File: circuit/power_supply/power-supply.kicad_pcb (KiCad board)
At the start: 2 copper layers, 21 parts, among them P1 CONN_2, U1 MCS34063A

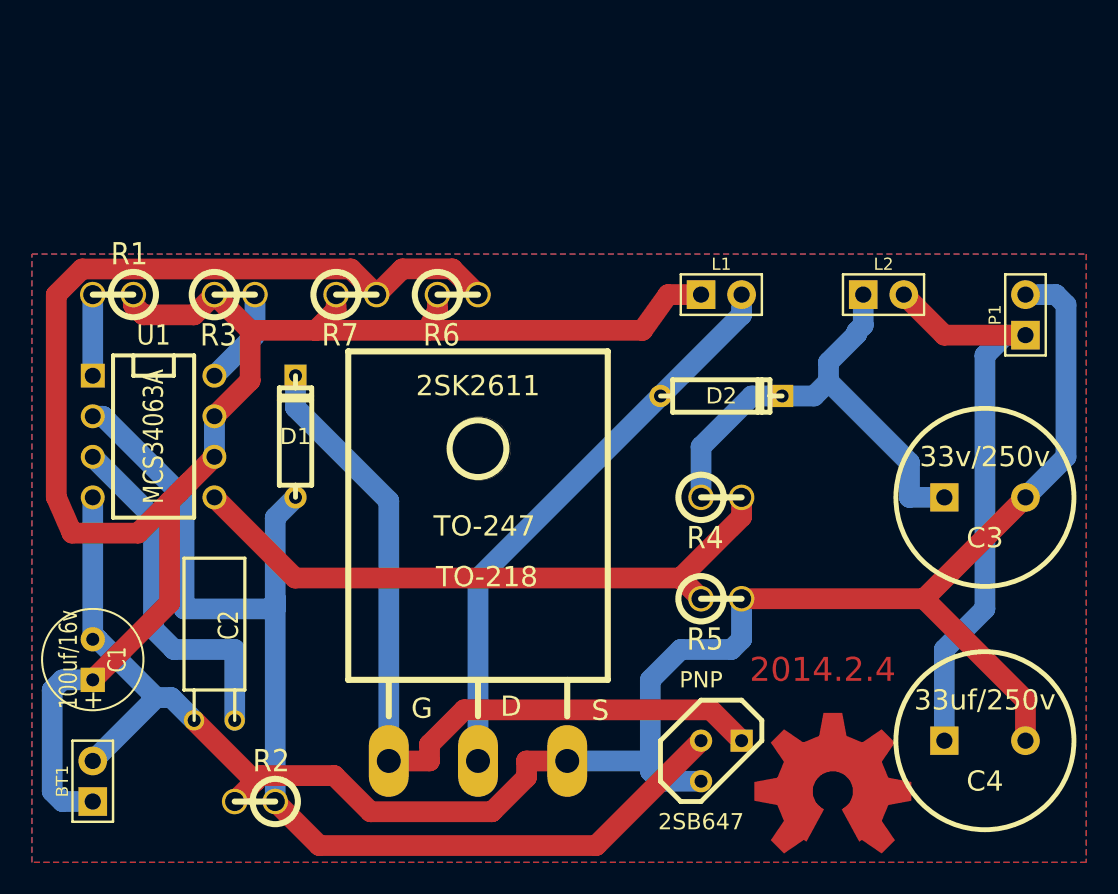
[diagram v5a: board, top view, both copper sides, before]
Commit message: power_supply: expanded the pad size
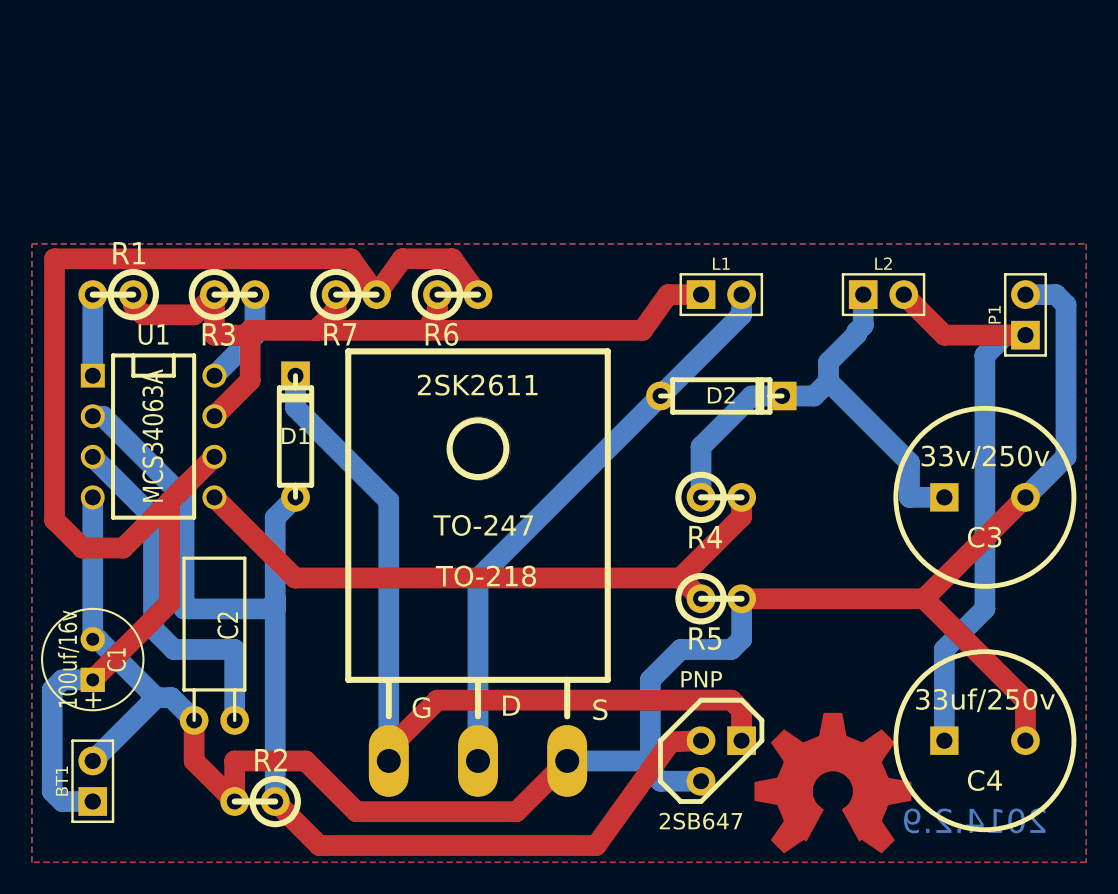
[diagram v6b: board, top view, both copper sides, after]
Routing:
- net N-0000011: track 80.2 -> 84.6 mm
- net N-000007: track 124.2 -> 126.6 mm
- net N-000004: track 51.4 -> 52.8 mm
- net N-000009: track 52.4 -> 51.8 mm
- net N-000008: track 71.9 -> 72.5 mm
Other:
- net class width 1.0 added: clearance 0.254, trace_width 1, via_dia 0.889, via_drill 0.635
- board text added: "2014.2.9"
- board text removed: "2014.2.4"

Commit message: power_supply: fixed the wrong TO-92 ECB footprint issue
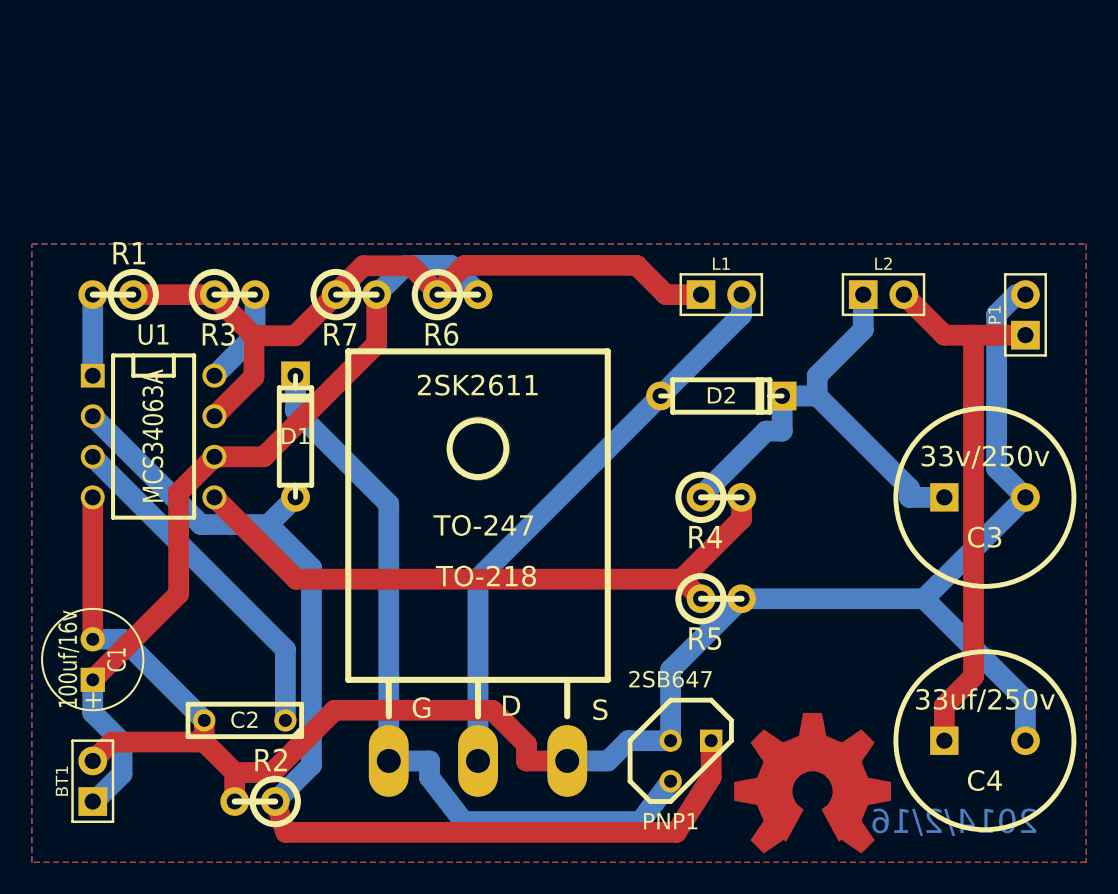
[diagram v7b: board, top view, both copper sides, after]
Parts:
- removed 2SB647: PNP, TO92
- added PNP1: 2SB647, TO92-123, F.Cu at (156.8, 121.9)
- C2: footprint QMONTRE -> C2
- moved C2 1.91 mm to (128.9, 119.4)
- moved OSHW_COPPER_10MM 1.27 mm to (164.5, 123.8)
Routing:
- net N-0000011: track 84.6 -> 50.4 mm
- net N-000001: track 126.6 -> 119.9 mm
- net N-000005: track 52.8 -> 47.9 mm
- net N-000009: track 51.8 -> 46.9 mm
- net N-000008: track 72.5 -> 68.5 mm
- net N-000006: track 36.9 -> 34.8 mm
- net N-000003: track 30.7 -> 29.7 mm
- net N-0000012: track 22.4 -> 21.5 mm
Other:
- board text added: "2014/2/16"
- board text removed: "2014.2.9"

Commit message: power_supply: expanded the pad size
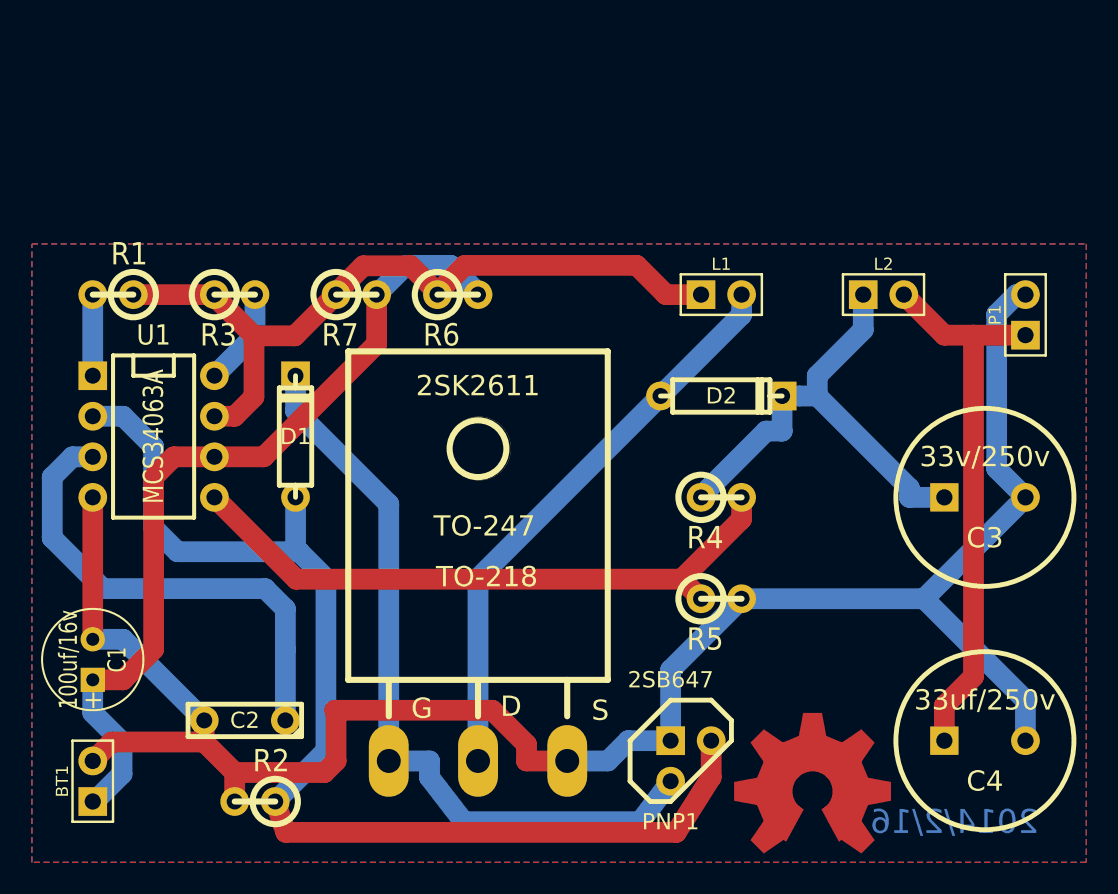
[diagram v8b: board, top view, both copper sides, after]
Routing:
- net N-0000012: track 21.5 -> 30.3 mm
- net N-000008: track 68.5 -> 73.4 mm
- net N-0000011: track 50.4 -> 53.1 mm
- net N-000001: track 119.9 -> 121.8 mm
- net N-000009: track 46.9 -> 47.7 mm
